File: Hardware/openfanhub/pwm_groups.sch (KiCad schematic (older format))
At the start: 3 parts, among them J4 Conn_01x04_Male, J5 Conn_01x04_Male, J6 Conn_01x04_Male

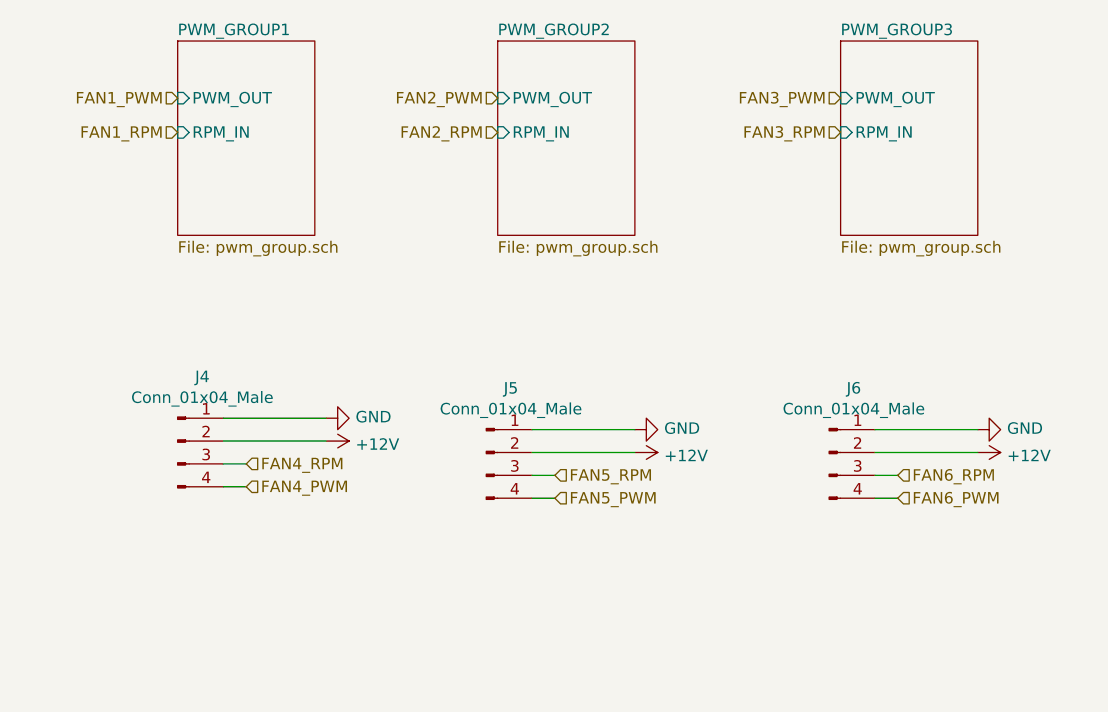
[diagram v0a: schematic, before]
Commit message: Update schematics with new pin layout
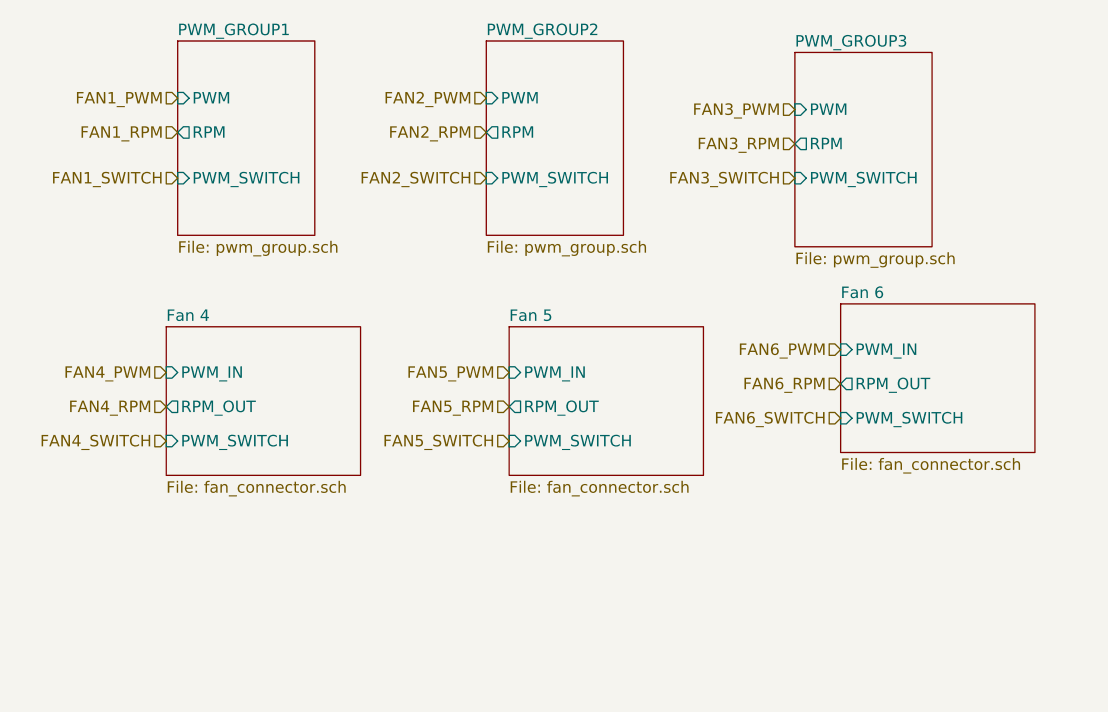
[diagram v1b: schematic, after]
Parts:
- removed J4, J5, J6: Conn_01x04_Male, Connector_PinHeader_2.54mm:PinHeader_1x04_P2.54mm_Horizontal, symbol Connector:Conn_01x04_Male

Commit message: Update files to kicad 6
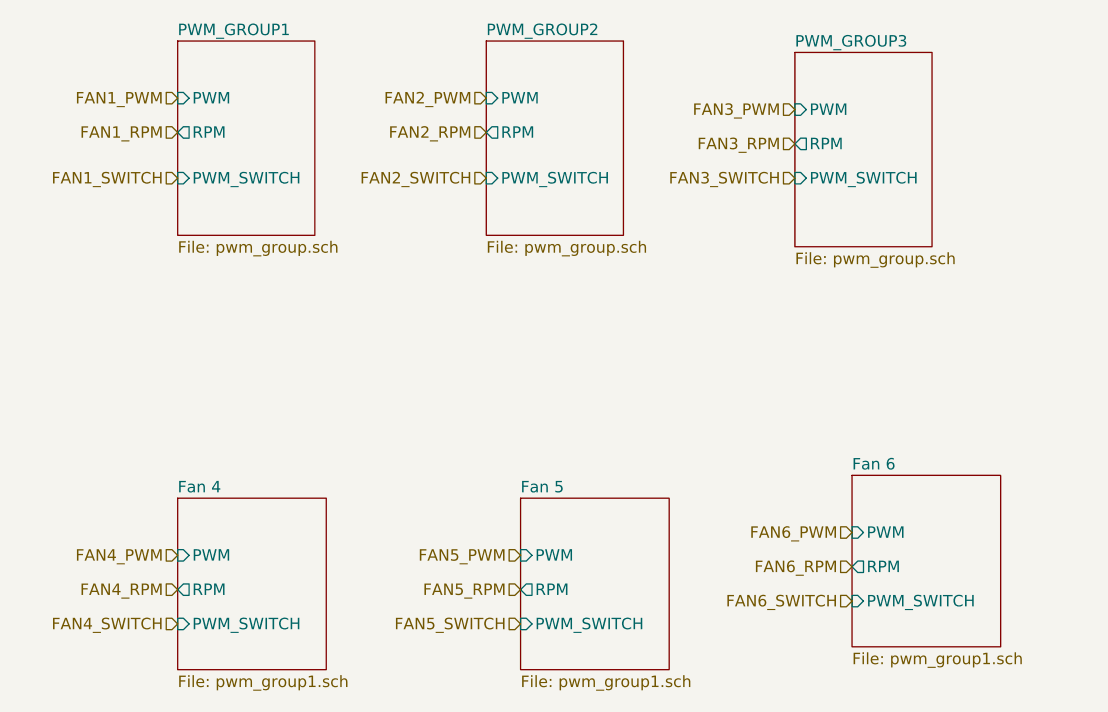
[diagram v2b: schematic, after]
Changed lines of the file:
@@
 $Descr A4 11693 8268
 encoding utf-8
-Sheet 2 17
+Sheet 2 20
 Title ""
 Date ""
@@
 Text HLabel 1100 1150 0    50   Input ~ 0
 FAN1_RPM
-$Sheet
-S 1050 2000 850  650
-U 61C9BC3A
-F0 "Fan 4" 50
-F1 "fan_connector.sch" 50
-F2 "PWM_IN" I L 1050 2200 50
-F3 "RPM_OUT" O L 1050 2350 50
-F4 "PWM_SWITCH" I L 1050 2500 50
-$EndSheet
 $Sheet
 S 1100 750  600  850
@@
 F4 "PWM_SWITCH" I L 3800 1350 50
 $EndSheet
-Text HLabel 1050 2200 0    50   Input ~ 0
+Text HLabel 1100 3000 0    50   Input ~ 0
 FAN4_PWM
-Text HLabel 1050 2350 0    50   Input ~ 0
+Text HLabel 1100 3150 0    50   Input ~ 0
 FAN4_RPM
-$Sheet
-S 2550 2000 850  650
-U 61CAFAB2
-F0 "Fan 5" 50
-F1 "fan_connector.sch" 50
-F2 "PWM_IN" I L 2550 2200 50
-F3 "RPM_OUT" O L 2550 2350 50
-F4 "PWM_SWITCH" I L 2550 2500 50
-$EndSheet
-Text HLabel 2550 2200 0    50   Input ~ 0
+Text HLabel 2600 3000 0    50   Input ~ 0
 FAN5_PWM
-Text HLabel 2550 2350 0    50   Input ~ 0
+Text HLabel 2600 3150 0    50   Input ~ 0
 FAN5_RPM
-$Sheet
-S 4000 1900 850  650
-U 61CAFCBB
-F0 "Fan 6" 50
-F1 "fan_connector.sch" 50
-F2 "PWM_IN" I L 4000 2100 50
-F3 "RPM_OUT" O L 4000 2250 50
-F4 "PWM_SWITCH" I L 4000 2400 50
-$EndSheet
-Text HLabel 4000 2100 0    50   Input ~ 0
+Text HLabel 4050 2900 0    50   Input ~ 0
 FAN6_PWM
-Text HLabel 4000 2250 0    50   Input ~ 0
+Text HLabel 4050 3050 0    50   Input ~ 0
 FAN6_RPM
 Text HLabel 1100 1350 0    50   Input ~ 0
@@
 Text HLabel 3800 1350 0    50   Input ~ 0
 FAN3_SWITCH
-Text HLabel 1050 2500 0    50   Input ~ 0
+Text HLabel 1100 3300 0    50   Input ~ 0
 FAN4_SWITCH
-Text HLabel 2550 2500 0    50   Input ~ 0
+Text HLabel 2600 3300 0    50   Input ~ 0
 FAN5_SWITCH
-Text HLabel 4000 2400 0    50   Input ~ 0
+Text HLabel 4050 3200 0    50   Input ~ 0
 FAN6_SWITCH
+$Sheet
+S 1100 2750 650  750
+U 61D07668
+F0 "Fan 4" 50
+F1 "pwm_group1.sch" 50
+F2 "PWM" I L 1100 3000 50
+F3 "RPM" O L 1100 3150 50
+F4 "PWM_SWITCH" I L 1100 3300 50
+$EndSheet
+$Sheet
+S 2600 2750 650  750
+U 61D0E238
+F0 "Fan 5" 50
+F1 "pwm_group1.sch" 50
+F2 "PWM" I L 2600 3000 50
+F3 "RPM" O L 2600 3150 50
+F4 "PWM_SWITCH" I L 2600 3300 50
+$EndSheet
+$Sheet
+S 4050 2650 650  750
+U 61D0E3A2
+F0 "Fan 6" 50
+F1 "pwm_group1.sch" 50
+F2 "PWM" I L 4050 2900 50
+F3 "RPM" O L 4050 3050 50
+F4 "PWM_SWITCH" I L 4050 3200 50
+$EndSheet
 $EndSCHEMATC
